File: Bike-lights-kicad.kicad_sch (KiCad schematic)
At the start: 1 part

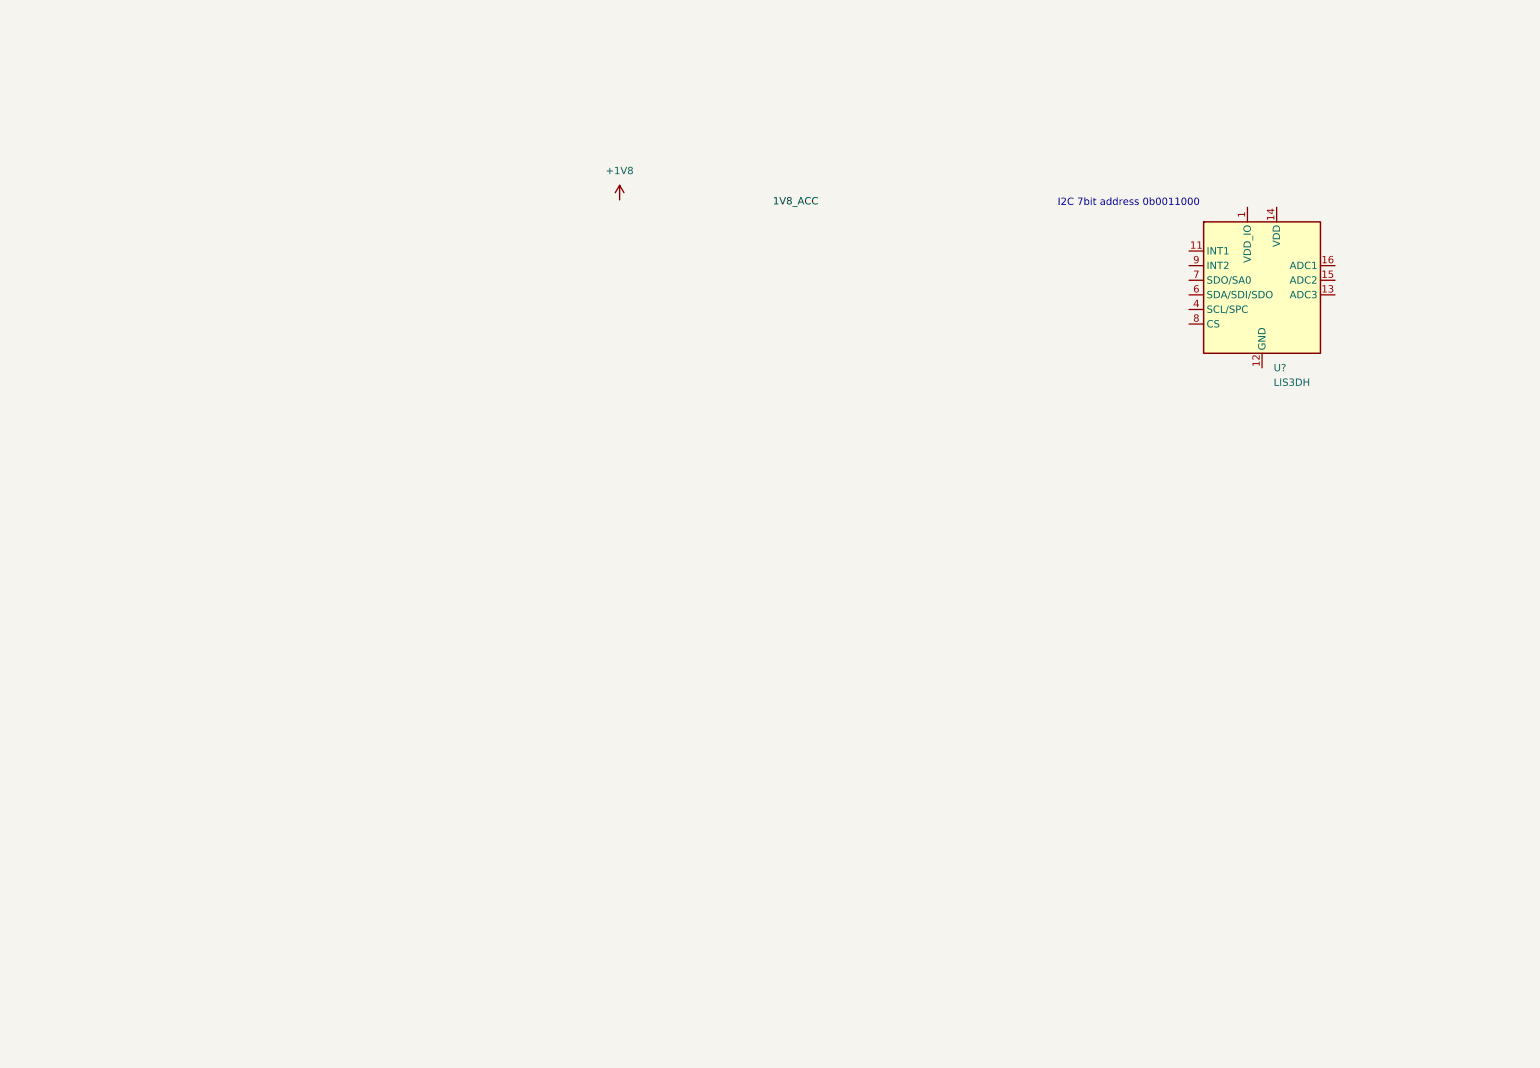
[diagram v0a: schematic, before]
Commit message: finished schematic and footprint assignment
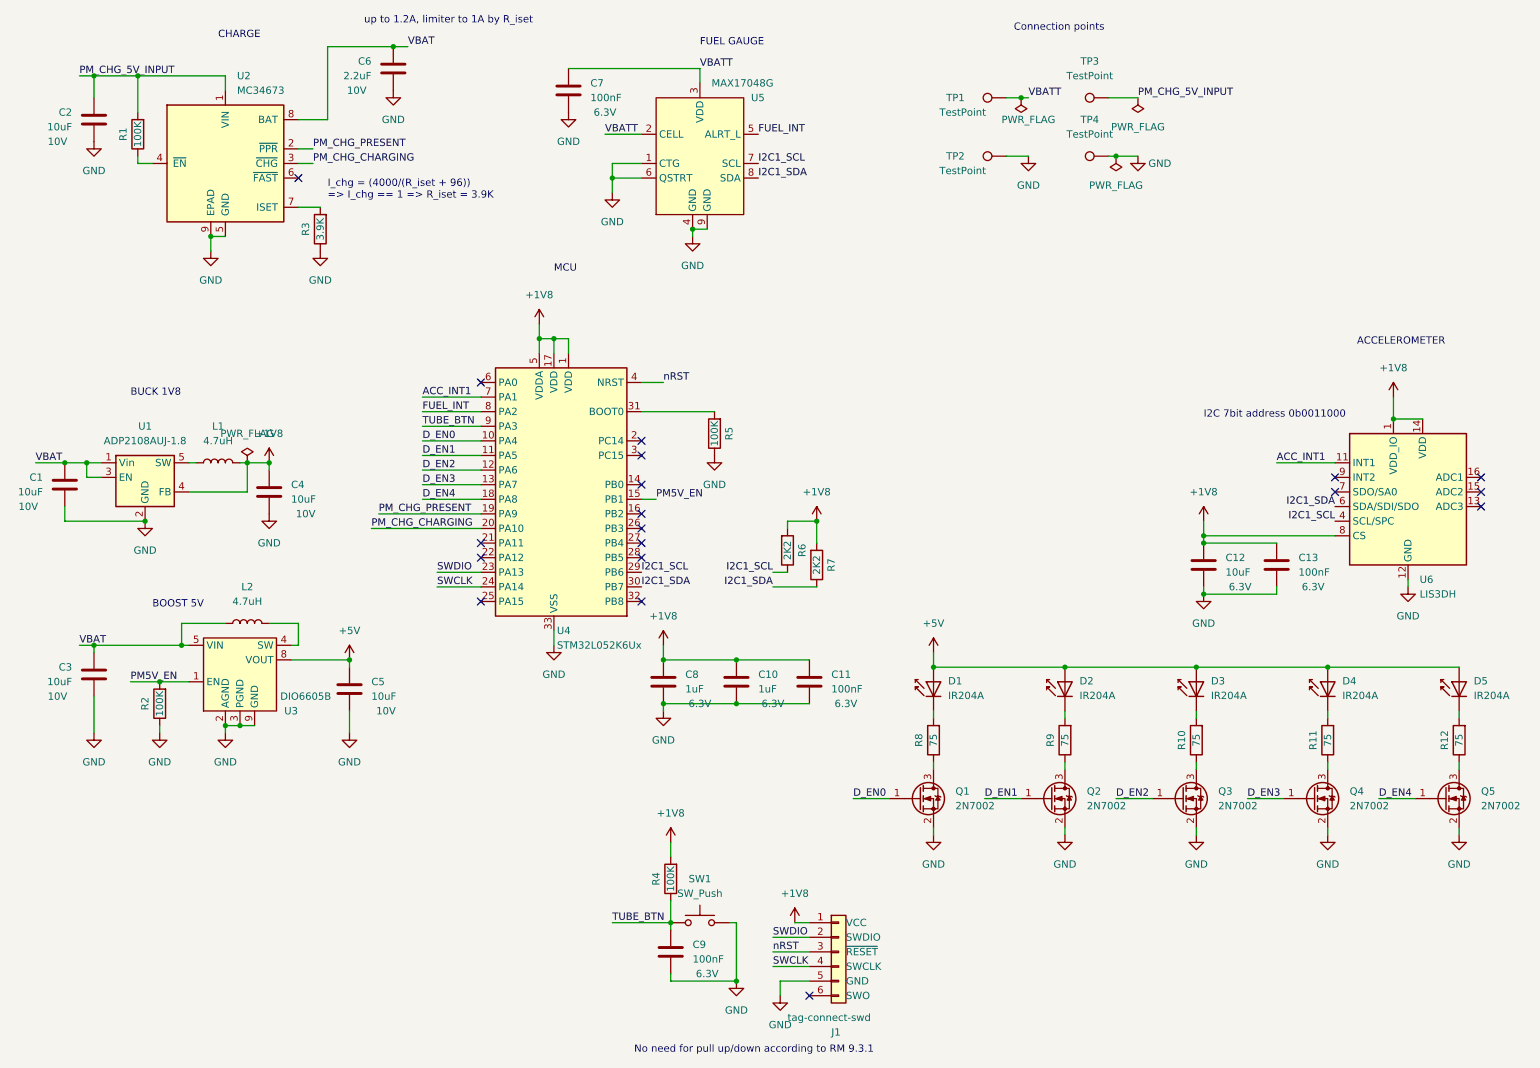
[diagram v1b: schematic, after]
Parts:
- added C1, C12, C2, C3, C4, C5: 10uF, Capacitor_SMD:C_0805_2012Metric, symbol Device:C
- added C10, C8: 1uF, Capacitor_SMD:C_0603_1608Metric, symbol Device:C
- added C11, C13, C7, C9: 100nF, Capacitor_SMD:C_0603_1608Metric, symbol Device:C
- added C6: 2.2uF, Capacitor_SMD:C_0805_2012Metric, symbol Device:C
- added D1, D2, D3, D4, D5: IR204A, LED_THT:LED_D3.0mm_IRBlack, symbol LED:IR204A
- added J1: tag-connect-swd, Connector:Tag-Connect_TC2030-IDC-NL_2x03_P1.27mm_Vertical, symbol connectors:tag-connect-swd
- added L1, L2: 4.7uH, Inductor_SMD:L_Taiyo-Yuden_NR-40xx, symbol Device:L
- added Q1, Q2, Q3, Q4, Q5: 2N7002, Package_TO_SOT_SMD:SOT-23, symbol Transistor_FET:2N7002
- added R1, R2, R4, R5: 100K, Resistor_SMD:R_0603_1608Metric, symbol Device:R
- added R10, R11, R12, R8, R9: 75, Resistor_SMD:R_0603_1608Metric, symbol Device:R
- added R3: 3.9K, Resistor_SMD:R_0603_1608Metric, symbol Device:R
- added R6, R7: 2K2, Resistor_SMD:R_0603_1608Metric, symbol Device:R
- added SW1: SW_Push, Button_Switch_SMD:SW_Push_1P1T_NO_CK_KSC6xxJ, symbol Switch:SW_Push
- added TP1, TP2, TP3, TP4: TestPoint, TestPoint:TestPoint_Pad_4.0x4.0mm, symbol Connector:TestPoint
- added U1: ADP2108AUJ-1.8, Package_TO_SOT_SMD:TSOT-23-5, symbol Regulator_Switching:ADP2108AUJ-1.8
- added U2: MC34673, Package_DFN_QFN:DFN-8-1EP_3x2mm_P0.5mm_EP1.75x1.45mm, symbol Battery_Management:MC34673
- added U3: DIO6605B, Package_DFN_QFN:TDFN-8-1EP_3x2mm_P0.5mm_EP1.4x1.4mm, symbol dc_dc_regulators:DIO6605B
- added U4: STM32L052K6Ux, Package_DFN_QFN:QFN-32-1EP_5x5mm_P0.5mm_EP3.45x3.45mm, symbol MCU_ST_STM32L0:STM32L052K6Ux
- added U5: MAX17048G, Package_DFN_QFN:WDFN-8-1EP_2x2mm_P0.5mm_EP0.8x1.2mm, symbol battery_management:MAX17048G
- gave numbers to parts that had none: 1
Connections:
- net +1V8: now also U6.1 (VDD_IO), U6.14 (VDD), U6.8 (CS), C10.1, C11.1, C12.1, C13.1, C4.1, C8.1, J1.1 (VCC), L1.2, R4.2, R6.2, R7.2, U1.4 (FB), U4.1 (VDD), U4.17 (VDD), U4.5 (VDDA)
- net GND: now reaches U6.10 (GND), U6.12 (GND), U6.5 (GND)
- net GND: now also C1.2, C10.2, C11.2, C12.2, C13.2, C2.2, C3.2, C4.2, C5.2, C6.2, C7.2, C8.2, C9.2, J1.5 (GND), Q1.2 (S), Q2.2 (S), Q3.2 (S), Q4.2 (S), Q5.2 (S), R2.1, R3.1, R5.1, SW1.2, TP2.1, TP4.1, U1.2 (GND), U2.5 (GND), U2.9 (EPAD), U3.2 (AGND), U3.3 (PGND), U3.9 (GND), U4.33 (VSS), U5.1 (CTG), U5.4 (GND), U5.6 (QSTRT), U5.9 (GND)
- net ACC_INT1: now reaches U6.11 (INT1)
- net ACC_INT1: now also U4.7 (PA1)
- net I2C1_SCL: now reaches U6.4 (SCL/SPC)
- net I2C1_SCL: now also R6.1, U4.29 (PB6), U5.7 (SCL)
- net I2C1_SDA: now reaches U6.6 (SDA/SDI/SDO)
- net I2C1_SDA: now also R7.1, U4.30 (PB7), U5.8 (SDA)
- new net: D3.1 (K), R10.2
- new net: R1.1, U2.4 (~{EN})
- new net: R3.2, U2.7 (ISET)
- new net: Q4.3 (D), R11.1
- new net: D1.1 (K), R8.2
- new net: Q2.3 (D), R9.1
- new net: D2.1 (K), R9.2
- new net: Q3.3 (D), R10.1
- new net: Q5.3 (D), R12.1
- new net: Q1.3 (D), R8.1
- new net: L1.1, U1.5 (SW)
- new net: R5.2, U4.31 (BOOT0)
- new net: D4.1 (K), R11.2
- new net: L2.2, U3.4 (SW)
- new net: D5.1 (K), R12.2
- new net +5V: C5.1, D1.2 (A), D2.2 (A), D3.2 (A), D4.2 (A), D5.2 (A), U3.8 (VOUT)
- new net D_EN0: Q1.1 (G), U4.10 (PA4)
- new net D_EN1: Q2.1 (G), U4.11 (PA5)
- new net D_EN2: Q3.1 (G), U4.12 (PA6)
- new net D_EN3: Q4.1 (G), U4.13 (PA7)
- new net D_EN4: Q5.1 (G), U4.18 (PA8)
- new net FUEL_INT: U4.8 (PA2), U5.5 (ALRT_L)
- new net PM5V_EN: R2.2, U3.1 (EN), U4.15 (PB1)
- new net PM_CHG_5V_INPUT: C2.1, R1.2, TP3.1, U2.1 (VIN)
- new net PM_CHG_CHARGING: U2.3 (~{CHG}), U4.20 (PA10)
- new net PM_CHG_PRESENT: U2.2 (~{PPR}), U4.19 (PA9)
- new net SWCLK: J1.4 (SWCLK), U4.24 (PA14)
- new net SWDIO: J1.2 (SWDIO), U4.23 (PA13)
- new net TUBE_BTN: C9.1, R4.1, SW1.1, U4.9 (PA3)
- new net VBAT: C1.1, C3.1, C6.1, L2.1, U1.1 (Vin), U1.3 (EN), U2.8 (BAT), U3.5 (VIN)
- new net VBATT: C7.1, TP1.1, U5.2 (CELL), U5.3 (VDD)
- new net nRST: J1.3 (~{RESET}), U4.4 (NRST)
- no-connect marks 0 -> 19
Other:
- note added: "ACCELEROMETER"
- note added: "BOOST 5V"
- note added: "BUCK 1V8"
- note added: "CHARGE"
- note added: "Connection points"
- note added: "FUEL GAUGE"
- note added: "I_chg = (4000/(R_iset + 96)) => I_chg == 1 => R_iset = 3.9K"
- note added: "MCU"
- note added: "No need for pull up/down according to RM 9.3.1"
- note added: "up to 1.2A, limiter to 1A by R_iset"
- moved on the sheet: U6

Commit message: output ready
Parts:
- removed R1: 100K, Resistor_SMD:R_0603_1608Metric, symbol Device:R
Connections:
- net VBATT is gone; now on net VBAT: C7.1, TP1.1, U5.2 (CELL), U5.3 (VDD)
- net +5V: now also U3.7 (VOUT); no longer U3.8 (VOUT)
- net PM_CHG_5V_INPUT: now also U2.4 (~{EN})
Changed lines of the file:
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@@
   (junction (at 180.34 130.81) (diameter 0) (color 0 0 0 0)
-  )
-  (junction (at 195.58 31.75) (diameter 0) (color 0 0 0 0)
   )
   (junction (at 260.35 87.63) (diameter 0) (color 0 0 0 0)
@@
     (stroke (width 0) (type default) (color 0 0 0 0))
   )
-  (wire (pts (xy 196.85 31.75) (xy 195.58 31.75))
+  (wire (pts (xy 193.04 31.75) (xy 196.85 31.75))
     (stroke (width 0) (type default) (color 0 0 0 0))
   )
@@
     (stroke (width 0) (type default) (color 0 0 0 0))
   )
-  (wire (pts (xy 195.58 31.75) (xy 193.04 31.75))
-    (stroke (width 0) (type default) (color 0 0 0 0))
-  )
   (wire (pts (xy 78.74 138.43) (xy 78.74 142.24))
     (stroke (width 0) (type default) (color 0 0 0 0))
@@
     (stroke (width 0) (type default) (color 0 0 0 0))
   )
-  (wire (pts (xy 41.91 43.18) (xy 41.91 41.91))
-    (stroke (width 0) (type default) (color 0 0 0 0))
-  )
   (wire (pts (xy 240.03 95.25) (xy 250.19 95.25))
     (stroke (width 0) (type default) (color 0 0 0 0))
@@
     (stroke (width 0) (type default) (color 0 0 0 0))
   )
-  (wire (pts (xy 41.91 27.94) (xy 41.91 34.29))
+  (wire (pts (xy 41.91 27.94) (xy 41.91 43.18))
     (stroke (width 0) (type default) (color 0 0 0 0))
   )
@@
     (effects (font (size 1.27 1.27)) (justify left bottom))
   )
-  (label "VBATT" (at 123.19 38.1 0)
-    (effects (font (size 1.27 1.27)) (justify left bottom))
-  )
-  (label "VBATT" (at 196.85 31.75 0)
+  (label "VBAT" (at 123.19 38.1 0)
+    (effects (font (size 1.27 1.27)) (justify left bottom))
+  )
+  (label "VBAT" (at 196.85 31.75 0)
     (effects (font (size 1.27 1.27)) (justify left bottom))
   )
@@
     (effects (font (size 1.27 1.27)) (justify left bottom))
   )
-  (label "VBATT" (at 139.7 26.67 0)
+  (label "VBAT" (at 139.7 26.67 0)
     (effects (font (size 1.27 1.27)) (justify left bottom))
   )
@@
     )
     (property "Datasheet" "" (id 3) (at 260.35 83.82 0)
-      (effects (font (size 1.27 1.27)) hide)
-    )
-    (pin "1")
-  )
-  (symbol (lib_id "power:PWR_FLAG") (at 195.58 31.75 180) (unit 1)
-    (in_bom yes) (on_board yes)
-    (property "Reference" "#FLG01" (id 0) (at 195.58 33.655 0)
-      (effects (font (size 1.27 1.27)) hide)
-    )
-    (property "Value" "PWR_FLAG" (id 1) (at 196.85 35.56 0))
-    (property "Footprint" "" (id 2) (at 195.58 31.75 0)
-      (effects (font (size 1.27 1.27)) hide)
-    )
-    (property "Datasheet" "~" (id 3) (at 195.58 31.75 0)
       (effects (font (size 1.27 1.27)) hide)
     )
@@
     (property "Reference" "U3" (id 0) (at 68.58 138.43 0))
     (property "Value" "DIO6605B" (id 1) (at 71.12 135.89 0))
-    (property "Footprint" "Package_DFN_QFN:TDFN-8-1EP_3x2mm_P0.5mm_EP1.4x1.4mm" (id 2) (at 59.69 132.08 0)
+    (property "Footprint" "Package_DFN_QFN:TDFN-8-1EP_3x2mm_P0.5mm_EP1.4x1.4mm" (id 2) (at 60.96 121.92 0)
       (effects (font (size 1.27 1.27)) hide)
     )
@@
     (pin "5")
     (pin "6")
-    (pin "8")
+    (pin "7")
     (pin "8")
     (pin "9")
@@
     (pin "2")
   )
-  (symbol (lib_id "Device:R") (at 41.91 38.1 180) (unit 1)
-    (in_bom yes) (on_board yes)
-    (property "Reference" "R1" (id 0) (at 39.37 38.1 90))
-    (property "Value" "100K" (id 1) (at 41.91 38.1 90))
-    (property "Footprint" "Resistor_SMD:R_0603_1608Metric" (id 2) (at 43.688 38.1 90)
-      (effects (font (size 1.27 1.27)) hide)
-    )
-    (property "Datasheet" "~" (id 3) (at 41.91 38.1 0)
-      (effects (font (size 1.27 1.27)) hide)
-    )
-    (pin "1")
-    (pin "2")
-  )
   (symbol (lib_id "Device:R") (at 154.94 110.49 0) (mirror x) (unit 1)
     (in_bom yes) (on_board yes)
@@
   )
   (symbol_instances
-    (path "/00d69d67-0154-4b04-9d77-3c80b931b7cd"
-      (reference "#FLG01") (unit 1) (value "PWR_FLAG") (footprint "")
-    )
     (path "/d0ebad45-8623-4332-a48e-ec33583d2245"
       (reference "#FLG02") (unit 1) (value "PWR_FLAG") (footprint "")
@@
       (reference "Q5") (unit 1) (value "2N7002") (footprint "Package_TO_SOT_SMD:SOT-23")
     )
-    (path "/ee350a17-625b-45c8-ac40-d5861f835870"
-      (reference "R1") (unit 1) (value "100K") (footprint "Resistor_SMD:R_0603_1608Metric")
-    )
     (path "/e246e83f-7cf7-43ab-a3fa-0b578e77b9fb"
